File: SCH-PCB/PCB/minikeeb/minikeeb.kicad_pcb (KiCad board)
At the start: 2 copper layers, 99.8 x 91 mm, 93 parts, among them J1 OLED, SW1 SW_PUSH-Lily58-cache, SW10 SW_PUSH-Lily58-cache, SW11 SW_PUSH-Lily58-cache, SW12 SW_PUSH-Lily58-cache, SW13 SW_PUSH-Lily58-cache, SW14 SW_PUSH-Lily58-cache, SW15 SW_PUSH-Lily58-cache, SW16 SW_PUSH-Lily58-cache, SW17 SW_PUSH-Lily58-cache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

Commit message: FEAT: update pcb
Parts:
- added J2: Conn_01x02_Pin, Connector_JST:JST_EH_B2B-EH-A_1x02_P2.50mm_Vertical, F.Cu at (36.4, 151.9)
- added J3: Conn_01x02_Pin, Connector_JST:JST_EH_B2B-EH-A_1x02_P2.50mm_Vertical, F.Cu at (54.2, 152.0)
- added S1: JS102011SAQN, other:SW_JS102011SAQN, F.Cu at (46.4, 152.6)
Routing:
- net Net-(J2-Pin_2): track 0.00 -> 20.9 mm
- net Net-(J3-Pin_1): track 0.00 -> 9.87 mm
- net Net-(J2-Pin_1): track 0.00 -> 8.89 mm
- net ench_a: track 30.0 -> 29.4 mm
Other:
- board size 99.8 x 91 mm -> 99.9 x 91 mm

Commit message: FEAT: update pcb for vcc selection
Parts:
- added JP13: Jumper_NO_Small, sofle:Jumper, F.Cu at (38.8, 142.5)
- added JP14: Jumper_NO_Small, sofle:Jumper, F.Cu at (38.7, 144.2)
- moved J2 0.25 mm to (36.2, 151.9)
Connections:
- U1 pad 21: VCC -> Net-(U1-VCC)
- U1 pad 24: unconnected-(U1-RAW-Pad24) -> Net-(U1-RAW)
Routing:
- net Net-(U1-RAW): track 0.00 -> 10.5 mm
- net txd0: track 91.6 -> 88.3 mm
- net rxd0: track 97.5 -> 94.2 mm
- net Net-(U1-VCC): track 0.00 -> 3.17 mm
- net VCC: track 600.7 -> 598.3 mm, vias 34 -> 35
- net GND: vias 83 -> 86
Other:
- outline, holes or cut-outs redrawn

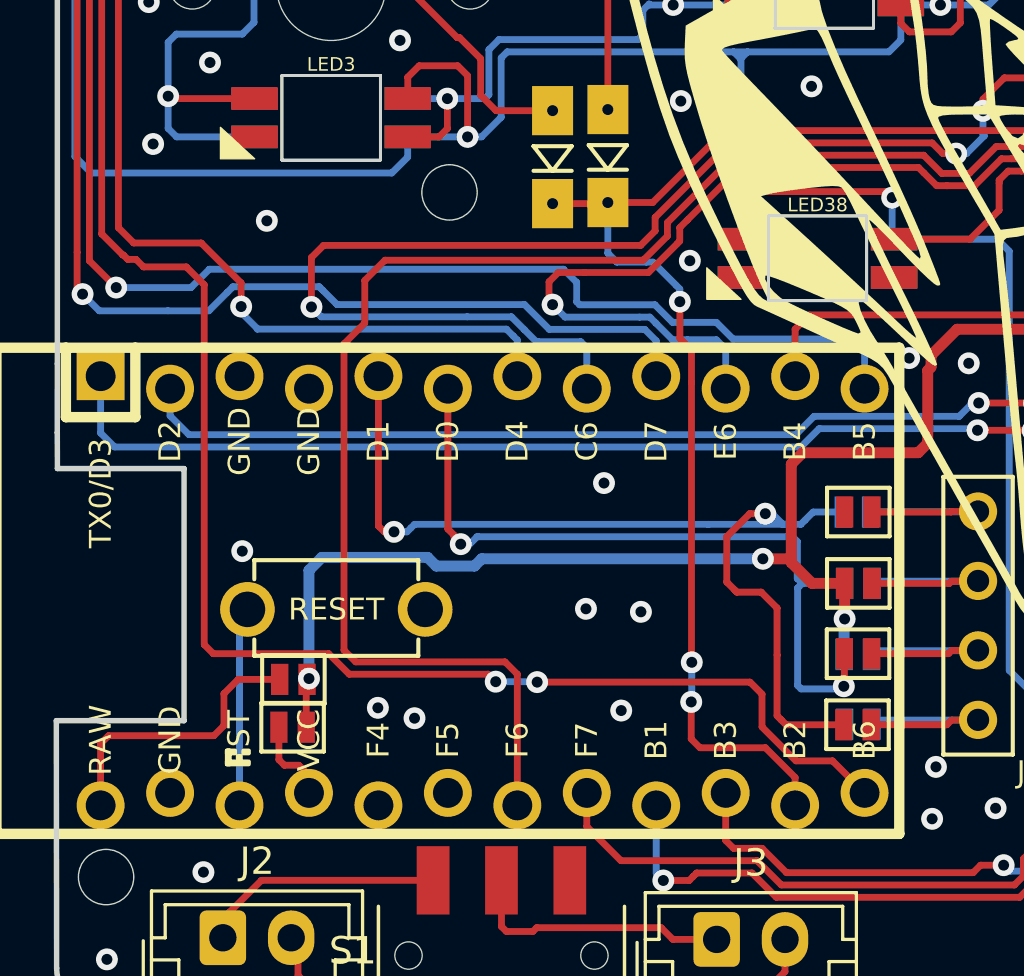
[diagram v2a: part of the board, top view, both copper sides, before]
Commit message: FEAT : update hole for plate design
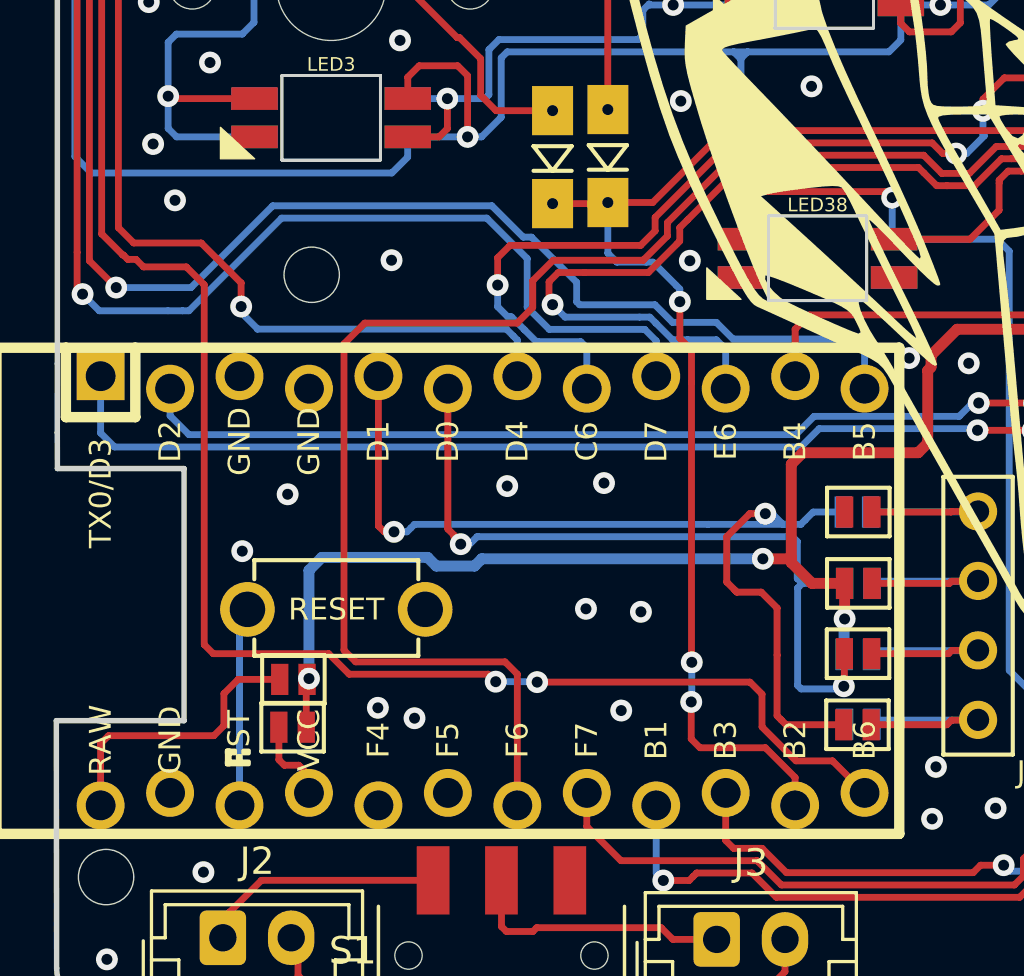
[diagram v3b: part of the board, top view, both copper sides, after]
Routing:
- net col1: track 96.0 -> 82.4 mm
- net din: track 73.7 -> 76.8 mm
- net row0: track 147.1 -> 149.1 mm
- net row1: track 140.4 -> 139.7 mm
- net GND: vias 86 -> 89
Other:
- outline, holes or cut-outs redrawn

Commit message: FIX fix dimension PCB
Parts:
- moved SW19 6.12 mm to (116.5, 119.1)
- moved LED17 5.73 mm to (116.5, 123.5)
- moved LED35 5.73 mm to (116.5, 123.5)
- moved D11 5.16 mm to (85.0, 149.9)
- moved LED16 5.04 mm to (116.6, 104.8)
- moved LED34 5.04 mm to (116.6, 104.8)
- moved SW15 5.02 mm to (97.2, 116.3)
- moved SW18 4.92 mm to (116.5, 100.1)
- moved LED12 4.89 mm to (97.3, 120.9)
- moved LED30 4.89 mm to (97.3, 120.9)
- moved SW11 4.60 mm to (78.3, 114.1)
- moved LED8 4.43 mm to (78.3, 118.7)
- moved LED26 4.43 mm to (78.3, 118.7)
- moved SW17 4.33 mm to (116.5, 81.1)
- moved LED33 4.27 mm to (116.4, 85.5)
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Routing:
- net VCC: track 598.3 -> 651.0 mm, vias 35 -> 36
- net col0: track 107.6 -> 68.3 mm, vias 5 -> 3
- net row1: track 139.7 -> 112.4 mm, vias 2 -> 3
- net row0: track 149.1 -> 122.1 mm, vias 1 -> 2
- net GND: track 1.49 -> 25.8 mm, vias 89 -> 90
- net col4: track 170.6 -> 193.6 mm, vias 10 -> 8
- net /10: track 37.8 -> 60.0 mm, vias 2 -> 3
- net row2: track 87.9 -> 102.0 mm
- net /15: track 57.1 -> 71.2 mm, vias 2 -> 4
- net /12: track 21.8 -> 33.1 mm, vias 2 -> 4
- net Net-(D11-A): track 10.2 -> 18.5 mm
- net col2: track 153.5 -> 146.0 mm, vias 8 -> 4
- net /2: track 23.9 -> 30.4 mm
- net col1: track 82.4 -> 88.1 mm, vias 8 -> 3
- net rxd0: track 94.2 -> 89.6 mm, vias 5 -> 1
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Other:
- board size 99.9 x 91 mm -> 99.9 x 94.6 mm

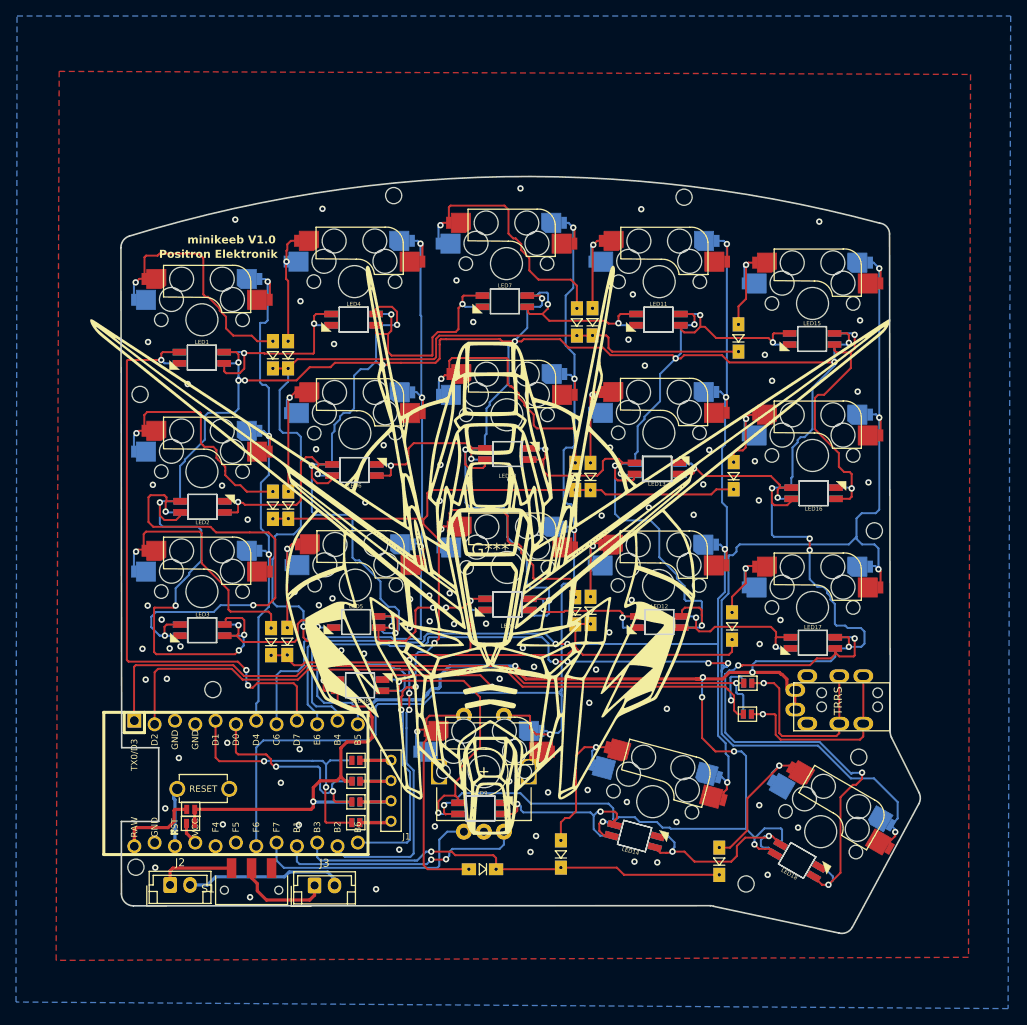
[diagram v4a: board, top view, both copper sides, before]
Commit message: FEAT: update keyboard pcb case and documentation
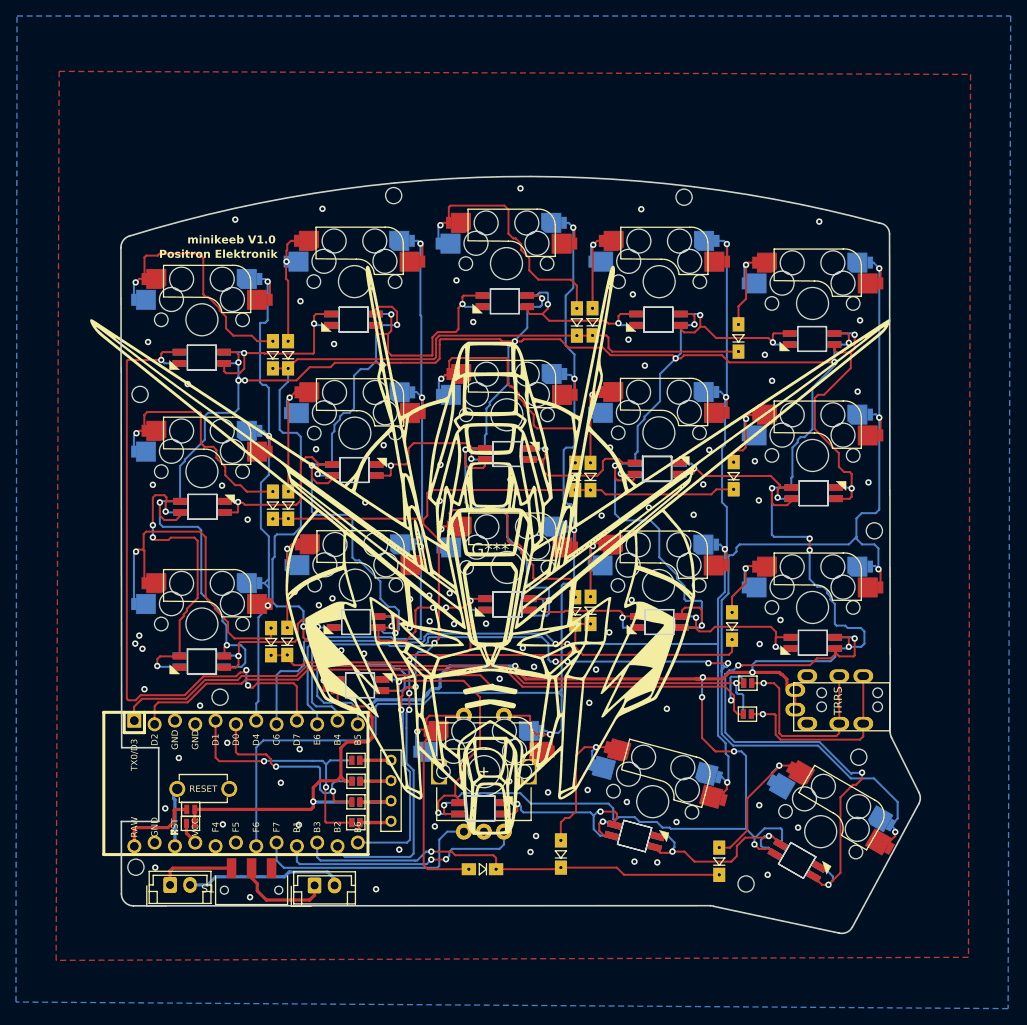
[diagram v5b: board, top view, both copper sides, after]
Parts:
- moved SW4 4.06 mm to (40.1, 121.2)
- moved LED3 3.98 mm to (40.1, 125.9)
- moved locked 3.88 mm to (40.1, 125.8)
- renumbered LED21 to locked
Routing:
- net /10: track 60.0 -> 40.3 mm, vias 3 -> 4
- net VCC: track 651.0 -> 635.5 mm, vias 36 -> 34
- net Net-(D3-A): track 31.6 -> 42.1 mm
- net din: track 75.7 -> 81.6 mm
- net txd0: track 90.3 -> 86.7 mm
- net rxd0: track 89.6 -> 87.3 mm
- net col0: track 68.3 -> 67.0 mm
- net /11: track 23.3 -> 24.5 mm
- net GND: vias 90 -> 88
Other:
- outline, holes or cut-outs redrawn
